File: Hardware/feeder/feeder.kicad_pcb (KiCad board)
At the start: 2 copper layers, 44.4 x 71.1 mm, 21 parts, among them J1 pump, J2 power, J3 button_set, J4 button_select, J5 button_reset, J6 motor, Q1 BUZ11

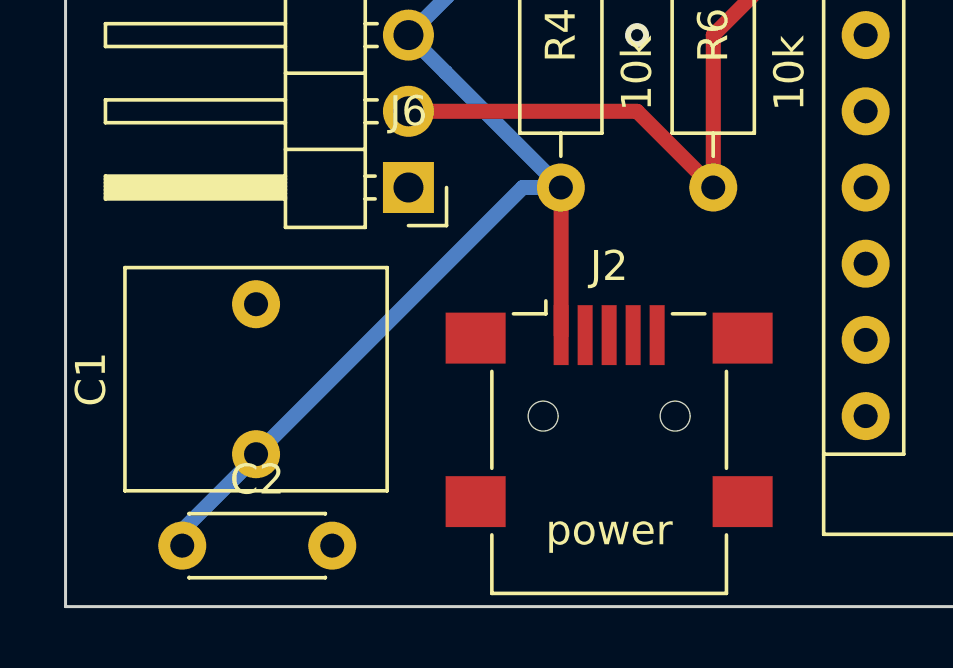
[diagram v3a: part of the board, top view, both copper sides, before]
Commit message: Change footprints of capacitors
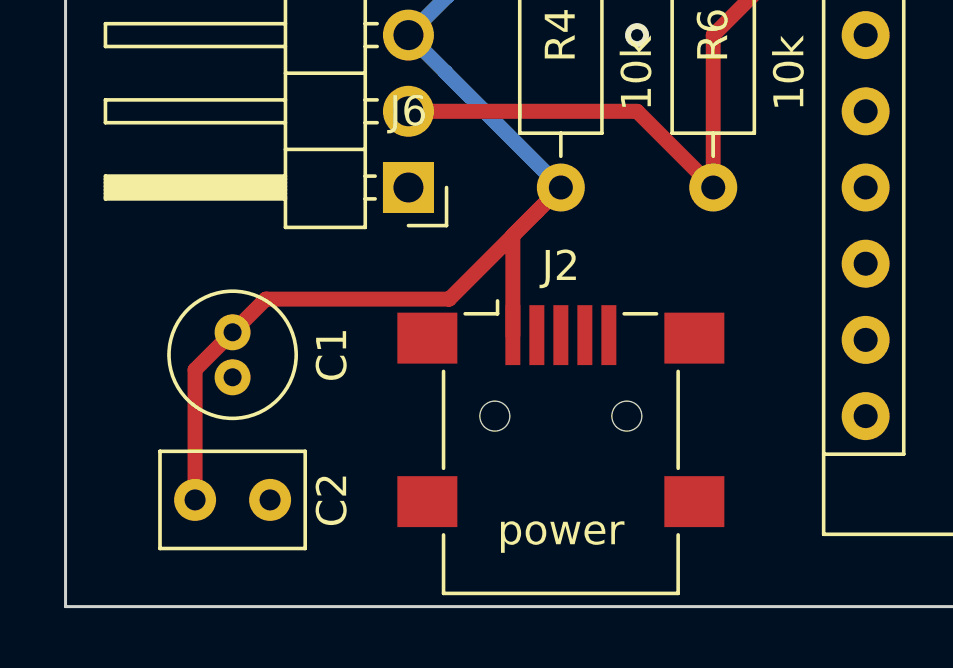
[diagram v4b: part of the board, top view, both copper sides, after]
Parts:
- C1: footprint Capacitor_THT:C_Rect_L7.2mm_W8.5mm_P5.00mm_FKP2_FKP2_MKS2_MKP2 -> Capacitor_THT:C_Radial_D4.0mm_H5.0mm_P1.50mm
- C2: footprint Capacitor_THT:C_Disc_D4.3mm_W1.9mm_P5.00mm -> Capacitor_THT:C_Rect_L4.6mm_W3.0mm_P2.50mm_MKS02_FKP02
- moved C1 4.14 mm to (118.6, 138.2), turned to 270 degrees
- moved J2 1.61 mm to (129.5, 141.0)
- moved C2 1.58 mm to (117.3, 143.8)
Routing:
- net +5V: track 100.8 -> 103.1 mm
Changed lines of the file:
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@@
     (thickness 1.6)
     (drawings 57)
-    (tracks 81)
+    (tracks 84)
     (zones 0)
     (modules 21)
@@
     (add_net "Net-(J2-Pad4)")
   )
-  (module Capacitor_THT:C_Rect_L7.2mm_W8.5mm_P5.00mm_FKP2_FKP2_MKS2_MKP2 (layer F.Cu)
-    (at 119.38 142.24 90)
-    (descr "C, Rect series, Radial, pin pitch=5.00mm, , length*width=7.2*8.5mm^2, Capacitor, http://www.wima.com/EN/WIMA_FKS_2.pdf")
-    (tags "C Rect series Radial pin pitch 5.00mm  length 7.2mm width 8.5mm Capacitor")
-    (fp_text reference C1 (at 2.5 -5.5 90) (layer F.SilkS)
-      (effects (font (size 1 1) (thickness 0.15)))
-    )
-    (fp_text value 4.7uF (at 2.5 5.5 90) (layer F.Fab)
-      (effects (font (size 1 1) (thickness 0.15)))
-    )
-    (fp_text user %R (at 2.5 0 90) (layer F.Fab)
-      (effects (font (size 1 1) (thickness 0.15)))
-    )
-    (fp_line (start 6.35 -4.5) (end -1.35 -4.5) (layer F.CrtYd) (width 0.05))
-    (fp_line (start 6.35 4.5) (end 6.35 -4.5) (layer F.CrtYd) (width 0.05))
-    (fp_line (start -1.35 4.5) (end 6.35 4.5) (layer F.CrtYd) (width 0.05))
-    (fp_line (start -1.35 -4.5) (end -1.35 4.5) (layer F.CrtYd) (width 0.05))
-    (fp_line (start 6.22 -4.37) (end 6.22 4.37) (layer F.SilkS) (width 0.12))
-    (fp_line (start -1.22 -4.37) (end -1.22 4.37) (layer F.SilkS) (width 0.12))
-    (fp_line (start -1.22 4.37) (end 6.22 4.37) (layer F.SilkS) (width 0.12))
-    (fp_line (start -1.22 -4.37) (end 6.22 -4.37) (layer F.SilkS) (width 0.12))
-    (fp_line (start 6.1 -4.25) (end -1.1 -4.25) (layer F.Fab) (width 0.1))
-    (fp_line (start 6.1 4.25) (end 6.1 -4.25) (layer F.Fab) (width 0.1))
-    (fp_line (start -1.1 4.25) (end 6.1 4.25) (layer F.Fab) (width 0.1))
-    (fp_line (start -1.1 -4.25) (end -1.1 4.25) (layer F.Fab) (width 0.1))
-    (pad 2 thru_hole circle (at 5 0 90) (size 1.6 1.6) (drill 0.8) (layers *.Cu *.Mask)
-      (net 22 GND))
-    (pad 1 thru_hole circle (at 0 0 90) (size 1.6 1.6) (drill 0.8) (layers *.Cu *.Mask)
+  (module Capacitor_THT:C_Rect_L4.6mm_W3.0mm_P2.50mm_MKS02_FKP02 (layer F.Cu)
+    (at 117.348 143.764)
+    (descr "C, Rect series, Radial, pin pitch=2.50mm, , length*width=4.6*3.0mm^2, Capacitor, http://www.wima.de/DE/WIMA_MKS_02.pdf")
+    (tags "C Rect series Radial pin pitch 2.50mm  length 4.6mm width 3.0mm Capacitor")
+    (fp_text reference C2 (at 4.572 0 90) (layer F.SilkS)
+      (effects (font (size 1 1) (thickness 0.15)))
+    )
+    (fp_text value 100nF (at 1.25 2.75) (layer F.Fab)
+      (effects (font (size 1 1) (thickness 0.15)))
+    )
+    (fp_text user %R (at 1.25 0) (layer F.Fab)
+      (effects (font (size 0.92 0.92) (thickness 0.138)))
+    )
+    (fp_line (start 3.8 -1.75) (end -1.3 -1.75) (layer F.CrtYd) (width 0.05))
+    (fp_line (start 3.8 1.75) (end 3.8 -1.75) (layer F.CrtYd) (width 0.05))
+    (fp_line (start -1.3 1.75) (end 3.8 1.75) (layer F.CrtYd) (width 0.05))
+    (fp_line (start -1.3 -1.75) (end -1.3 1.75) (layer F.CrtYd) (width 0.05))
+    (fp_line (start 3.67 -1.62) (end 3.67 1.62) (layer F.SilkS) (width 0.12))
+    (fp_line (start -1.17 -1.62) (end -1.17 1.62) (layer F.SilkS) (width 0.12))
+    (fp_line (start -1.17 1.62) (end 3.67 1.62) (layer F.SilkS) (width 0.12))
+    (fp_line (start -1.17 -1.62) (end 3.67 -1.62) (layer F.SilkS) (width 0.12))
+    (fp_line (start 3.55 -1.5) (end -1.05 -1.5) (layer F.Fab) (width 0.1))
+    (fp_line (start 3.55 1.5) (end 3.55 -1.5) (layer F.Fab) (width 0.1))
+    (fp_line (start -1.05 1.5) (end 3.55 1.5) (layer F.Fab) (width 0.1))
+    (fp_line (start -1.05 -1.5) (end -1.05 1.5) (layer F.Fab) (width 0.1))
+    (pad 2 thru_hole circle (at 2.5 0) (size 1.4 1.4) (drill 0.7) (layers *.Cu *.Mask)
+      (net 22 GND))
+    (pad 1 thru_hole circle (at 0 0) (size 1.4 1.4) (drill 0.7) (layers *.Cu *.Mask)
       (net 24 +5V))
-    (model ${KISYS3DMOD}/Capacitor_THT.3dshapes/C_Rect_L7.2mm_W8.5mm_P5.00mm_FKP2_FKP2_MKS2_MKP2.wrl
-      (at (xyz 0 0 0))
-      (scale (xyz 1 1 1))
-      (rotate (xyz 0 0 0))
-    )
-  )
-  (module Capacitor_THT:C_Disc_D4.3mm_W1.9mm_P5.00mm (layer F.Cu)
-    (at 116.92 145.288)
-    (descr "C, Disc series, Radial, pin pitch=5.00mm, , diameter*width=4.3*1.9mm^2, Capacitor, http://www.vishay.com/docs/45233/krseries.pdf")
-    (tags "C Disc series Radial pin pitch 5.00mm  diameter 4.3mm width 1.9mm Capacitor")
-    (fp_text reference C2 (at 2.5 -2.2) (layer F.SilkS)
-      (effects (font (size 1 1) (thickness 0.15)))
-    )
-    (fp_text value 100nF (at 2.5 2.2) (layer F.Fab)
-      (effects (font (size 1 1) (thickness 0.15)))
-    )
-    (fp_text user %R (at 2.5 0) (layer F.Fab)
-      (effects (font (size 0.86 0.86) (thickness 0.129)))
-    )
-    (fp_line (start 6.05 -1.2) (end -1.05 -1.2) (layer F.CrtYd) (width 0.05))
-    (fp_line (start 6.05 1.2) (end 6.05 -1.2) (layer F.CrtYd) (width 0.05))
-    (fp_line (start -1.05 1.2) (end 6.05 1.2) (layer F.CrtYd) (width 0.05))
-    (fp_line (start -1.05 -1.2) (end -1.05 1.2) (layer F.CrtYd) (width 0.05))
-    (fp_line (start 4.77 1.055) (end 4.77 1.07) (layer F.SilkS) (width 0.12))
-    (fp_line (start 4.77 -1.07) (end 4.77 -1.055) (layer F.SilkS) (width 0.12))
-    (fp_line (start 0.23 1.055) (end 0.23 1.07) (layer F.SilkS) (width 0.12))
-    (fp_line (start 0.23 -1.07) (end 0.23 -1.055) (layer F.SilkS) (width 0.12))
-    (fp_line (start 0.23 1.07) (end 4.77 1.07) (layer F.SilkS) (width 0.12))
-    (fp_line (start 0.23 -1.07) (end 4.77 -1.07) (layer F.SilkS) (width 0.12))
-    (fp_line (start 4.65 -0.95) (end 0.35 -0.95) (layer F.Fab) (width 0.1))
-    (fp_line (start 4.65 0.95) (end 4.65 -0.95) (layer F.Fab) (width 0.1))
-    (fp_line (start 0.35 0.95) (end 4.65 0.95) (layer F.Fab) (width 0.1))
-    (fp_line (start 0.35 -0.95) (end 0.35 0.95) (layer F.Fab) (width 0.1))
-    (pad 2 thru_hole circle (at 5 0) (size 1.6 1.6) (drill 0.8) (layers *.Cu *.Mask)
-      (net 22 GND))
-    (pad 1 thru_hole circle (at 0 0) (size 1.6 1.6) (drill 0.8) (layers *.Cu *.Mask)
+    (model ${KISYS3DMOD}/Capacitor_THT.3dshapes/C_Rect_L4.6mm_W3.0mm_P2.50mm_MKS02_FKP02.wrl
+      (at (xyz 0 0 0))
+      (scale (xyz 1 1 1))
+      (rotate (xyz 0 0 0))
+    )
+  )
+  (module Capacitor_THT:C_Radial_D4.0mm_H5.0mm_P1.50mm (layer F.Cu)
+    (at 118.598 138.176 270)
+    (descr "C, Radial series, Radial, pin pitch=1.50mm, diameter=4mm, height=5mm, Non-Polar Electrolytic Capacitor")
+    (tags "C Radial series Radial pin pitch 1.50mm diameter 4mm height 5mm Non-Polar Electrolytic Capacitor")
+    (fp_text reference C1 (at 0.75 -3.322 90) (layer F.SilkS)
+      (effects (font (size 1 1) (thickness 0.15)))
+    )
+    (fp_text value 4.7uF (at 0.75 3.25 90) (layer F.Fab)
+      (effects (font (size 1 1) (thickness 0.15)))
+    )
+    (fp_text user %R (at 0.75 0 90) (layer F.Fab)
+      (effects (font (size 0.8 0.8) (thickness 0.12)))
+    )
+    (fp_circle (center 0.75 0) (end 3 0) (layer F.CrtYd) (width 0.05))
+    (fp_circle (center 0.75 0) (end 2.87 0) (layer F.SilkS) (width 0.12))
+    (fp_circle (center 0.75 0) (end 2.75 0) (layer F.Fab) (width 0.1))
+    (pad 2 thru_hole circle (at 1.5 0 270) (size 1.2 1.2) (drill 0.6) (layers *.Cu *.Mask)
+      (net 22 GND))
+    (pad 1 thru_hole circle (at 0 0 270) (size 1.2 1.2) (drill 0.6) (layers *.Cu *.Mask)
       (net 24 +5V))
-    (model ${KISYS3DMOD}/Capacitor_THT.3dshapes/C_Disc_D4.3mm_W1.9mm_P5.00mm.wrl
+    (model ${KISYS3DMOD}/Capacitor_THT.3dshapes/C_Radial_D4.0mm_H5.0mm_P1.50mm.wrl
       (at (xyz 0 0 0))
       (scale (xyz 1 1 1))
@@
   )
   (module Connector_USB:USB_Mini-B_Lumberg_2486_01_Horizontal (layer F.Cu)
-    (at 131.15 140.97)
+    (at 129.54 140.97)
     (descr "USB Mini-B 5-pin SMD connector, http://downloads.lumberg.com/datenblaetter/en/2486_01.pdf")
     (tags "USB USB_B USB_Mini connector")
@@
   (segment (start 134.62 109.22) (end 137.240001 106.599999) (width 0.5) (layer B.Cu) (net 24))
   (segment (start 129.55 133.36) (end 129.54 133.35) (width 0.5) (layer F.Cu) (net 24))
-  (segment (start 129.55 138.27) (end 129.55 133.36) (width 0.5) (layer F.Cu) (net 24))
-  (segment (start 128.27 133.35) (end 119.38 142.24) (width 0.5) (layer B.Cu) (net 24))
-  (segment (start 129.54 133.35) (end 128.27 133.35) (width 0.5) (layer B.Cu) (net 24))
-  (segment (start 119.38 142.24) (end 119.38 142.32) (width 0.5) (layer B.Cu) (net 24) (status 1000000))
-  (segment (start 119.38 142.32) (end 116.92 144.78) (width 0.5) (layer B.Cu) (net 24) (status 1000000))
+  (segment (start 127.94 134.95) (end 129.54 133.35) (width 0.5) (layer F.Cu) (net 24))
+  (segment (start 127.94 138.27) (end 127.94 134.95) (width 0.5) (layer F.Cu) (net 24))
+  (segment (start 128.740001 134.149999) (end 129.54 133.35) (width 0.5) (layer F.Cu) (net 24))
+  (segment (start 125.820001 137.069999) (end 128.740001 134.149999) (width 0.5) (layer F.Cu) (net 24))
+  (segment (start 119.704001 137.069999) (end 125.820001 137.069999) (width 0.5) (layer F.Cu) (net 24))
+  (segment (start 118.598 138.176) (end 119.704001 137.069999) (width 0.5) (layer F.Cu) (net 24))
+  (segment (start 117.348 139.426) (end 117.348 143.764) (width 0.5) (layer F.Cu) (net 24))
+  (segment (start 118.598 138.176) (end 117.348 139.426) (width 0.5) (layer F.Cu) (net 24))
   (segment (start 128.27 101.6) (end 125.73 101.6) (width 0.5) (layer F.Cu) (net 27))
   (segment (start 125.73 101.6) (end 124.46 100.33) (width 0.5) (layer F.Cu) (net 27))
